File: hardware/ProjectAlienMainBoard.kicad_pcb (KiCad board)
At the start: 2 copper layers, 69.1 x 100.6 mm, 53 parts, among them J1 Bumper Connector, J3 Left Motor Connector, J4 Right Motor Connector, J5 Pixels Connector, J6 Ultrasonic Connector, J7 Micro USB, J8 I2C Multiplexer, J98 Voltage Breakout, J99 Excess GPIO Pins, Q1 2N3904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

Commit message: Fixed all errors
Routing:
- net +3.3V: track 248.6 -> 252.6 mm
- net ENC2A: track 43.3 -> 46.3 mm, vias 0 -> 2
- net Net-(A1-~{RESET}-Pad3): track 31.6 -> 34.6 mm
- net BUMPER_DATA: track 38.6 -> 37.1 mm
- net I2C_SCL: track 44.3 -> 45.2 mm

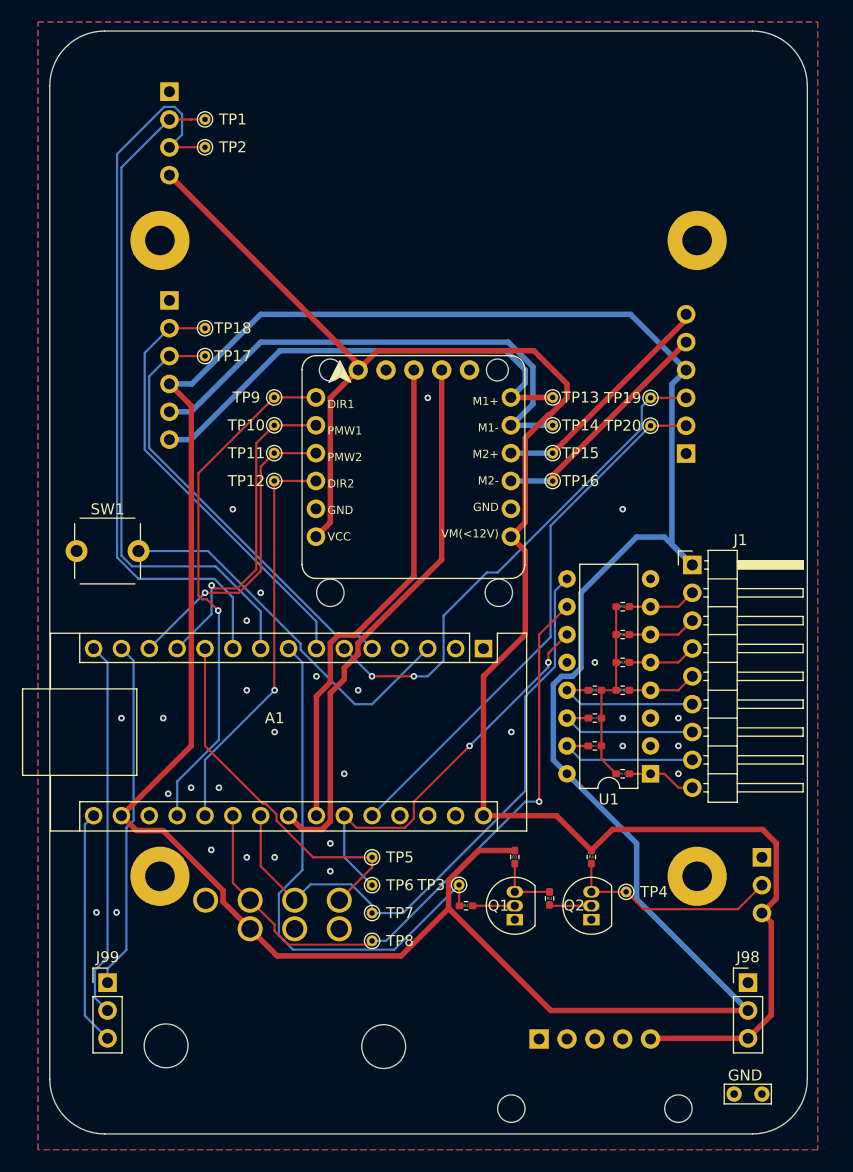
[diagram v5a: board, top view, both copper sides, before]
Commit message: Finished component silkscreen labels
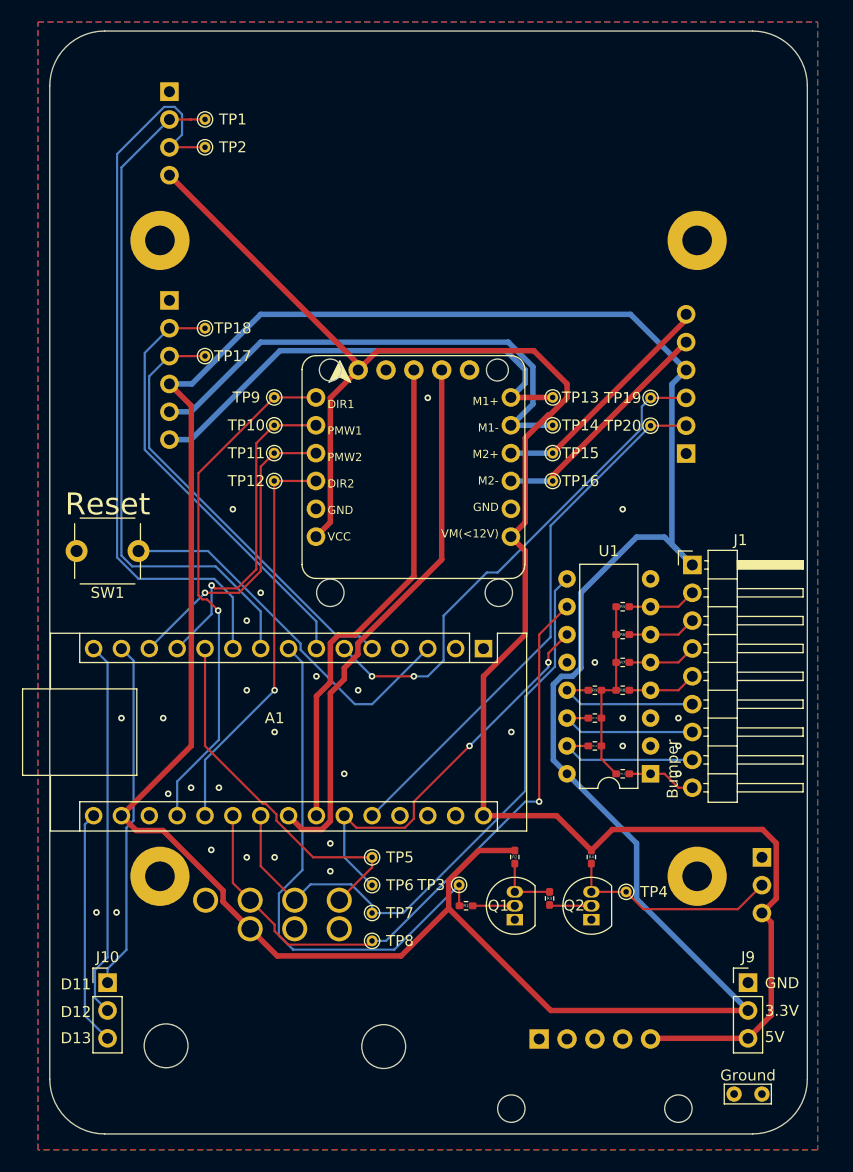
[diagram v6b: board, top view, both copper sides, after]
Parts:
- GND1: value GND -> Ground
- J1: value Bumper Connector -> Bumper
- J3: value Left Motor Connector -> Left Motor
- J4: value Right Motor Connector -> Right Motor
- J5: value Pixels Connector -> Pixels
- J6: value Ultrasonic Connector -> Ultrasonic
- SW1: value Reset Button -> Reset
- renumbered J99 to J10, J98 to J9
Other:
- board text added: "3.3V"
- board text added: "5V"
- board text added: "D11"
- board text added: "D12"
- board text added: "D13"
- board text added: "GND"
- board text added: "NES Port"
